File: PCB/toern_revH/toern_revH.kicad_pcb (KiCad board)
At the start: 4 copper layers, 160 x 71 mm, 130 parts, among them CN1 YZP0354-20100-01, CN2 YZP0354-20100-01, IC1 BQ24075TRGTR, J1 AudioJack3_Switch, J10 Conn_01x02, J11 Conn_01x05, J11.5 Conn_01x05, J12 Conn_01x05, J13 Conn_01x05, J14 Conn_01x05, J15 Conn_01x05, J16 Conn_01x02, J17 AudioJack3_Ground, J18 Conn_01x05_Socket, J19 Conn_01x05_Socket, J2 Conn_01x05_Socket, J20 Conn_01x05_Socket, J21 Conn_01x05_Socket, J22 Conn_01x05_Socket, J23 Conn_01x05_Socket, J24 Conn_01x05_Socket, J25 Conn_01x02, J26 Conn_01x02, J27 Conn_01x02, J28 929870-01-12-RA, J29 929870-01-12-RA, J3 AudioJack3_Ground, J30 929870-01-12-RA, J31 929870-01-12-RA, J4 USB_C_Receptacle_USB2.0, J5 AudioJack3_Switch, J6 AudioJack3_Switch, J7 AudioJack3_Switch, J8 Micro_SD_Card, J9 Conn_01x03, U1 SPX3819M5-L-3-3, U13 PAM8403D, U14 74LVC1G17, U15 74AHCT1G125, U16 74AHCT1G125, U2 SPX3819M5-L-1-8, U3 SGTL5000XNBA3, U4 TLP2361V4_E, U5 74LVC2G14, U6 Teensy4.1, U7 SPX3819M5-L-3-3, U8 TPS22918DBVR

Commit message: updated BAT45s Pins on PCB+Shematics
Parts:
- D2: value D_Schottky_Dual_Series_ACK -> BAT54S
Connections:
- D2 pad 2: Net-(D2-common) -> +3.3V
- D2 pad 3: +3.3V -> Net-(D2-common)
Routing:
- net Net-(D2-common): track 13.0 -> 11.5 mm
- net +3.3V: track 378.6 -> 377.5 mm, vias 17 -> 15
- net 38_CS1_IN1: track 17.9 -> 17.3 mm, vias 1 -> 0
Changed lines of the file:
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@@
 			)
 		)
-		(property "Value" "D_Schottky_Dual_Series_ACK"
+		(property "Value" "BAT54S"
 			(at 0 2.4 0)
 			(layer "F.Fab")
@@
 			)
 		)
-		(property "Datasheet" "~"
+		(property "Datasheet" "https://assets.nexperia.com/documents/data-sheet/BAT54S.pdf"
 			(at 0 0 0)
 			(layer "F.Fab")
@@
 			)
 		)
-		(property "Description" "Dual Schottky diode, anode/center/cathode"
+		(property "Description" "Dual series Schottky BAT54S: pin1=A, pin2=K, pin3=common"
 			(at 0 0 0)
 			(layer "F.Fab")
@@
 			(layers "F.Cu" "F.Mask" "F.Paste")
 			(roundrect_rratio 0.25)
-			(net 139 "Net-(D2-common)")
-			(pinfunction "common")
+			(net 7 "+3.3V")
+			(pinfunction "K")
 			(pintype "passive")
 		)
@@
 			(layers "F.Cu" "F.Mask" "F.Paste")
 			(roundrect_rratio 0.25)
-			(net 7 "+3.3V")
-			(pinfunction "K")
+			(net 139 "Net-(D2-common)")
+			(pinfunction "common")
 			(pintype "passive")
 		)
@@
 	)
 	(segment
+		(start 160.225 29.7)
+		(end 163.925 29.7)
+		(width 0.2)
+		(layer "F.Cu")
+		(net 7)
+	)
+	(segment
 		(start 72.5 50)
 		(end 73.5 50)
@@
 	)
 	(segment
+		(start 163.925 29.7)
+		(end 164.275 29.35)
+		(width 0.2)
+		(layer "F.Cu")
+		(net 7)
+	)
+	(segment
 		(start 161 66.25)
 		(end 178.125 66.25)
@@
 	)
 	(segment
-		(start 161.8 30.9)
-		(end 161.8 31.25)
-		(width 0.2)
-		(layer "F.Cu")
-		(net 7)
-	)
-	(segment
 		(start 184.6 66.25)
 		(end 187.55 63.3)
@@
 	)
 	(segment
-		(start 162.4 30.3)
-		(end 161.8 30.9)
-		(width 0.2)
-		(layer "F.Cu")
-		(net 7)
-	)
-	(segment
 		(start 118.22 75.78)
 		(end 118.22 77.5)
@@
 	)
 	(segment
-		(start 160.225 29.025)
-		(end 160.5 28.75)
-		(width 0.2)
-		(layer "F.Cu")
-		(net 7)
-	)
-	(segment
 		(start 121.22 75.505)
 		(end 121.225 75.5)
@@
 	)
 	(segment
-		(start 160.225 29.7)
-		(end 160.225 29.025)
-		(width 0.2)
-		(layer "F.Cu")
-		(net 7)
-	)
-	(segment
 		(start 117.325 80.325)
 		(end 118 81)
@@
 	)
 	(via
-		(at 161.8 31.25)
-		(size 0.5)
-		(drill 0.3)
-		(layers "F.Cu" "B.Cu")
-		(net 7)
-	)
-	(via
 		(at 146.465 39.615)
 		(size 0.5)
@@
 	)
 	(via
-		(at 160.5 28.75)
-		(size 0.5)
-		(drill 0.3)
-		(layers "F.Cu" "B.Cu")
-		(net 7)
-	)
-	(via
 		(at 143.7 51.45)
 		(size 0.5)
@@
 	)
 	(segment
-		(start 161.8 30.05)
-		(end 160.5 28.75)
-		(width 0.2)
-		(layer "B.Cu")
-		(net 7)
-	)
-	(segment
 		(start 72.5 50)
 		(end 72 50.5)
@@
 	)
 	(segment
-		(start 161.8 31.25)
-		(end 161.8 30.05)
-		(width 0.2)
-		(layer "B.Cu")
-		(net 7)
-	)
-	(segment
 		(start 80.5 41.69)
 		(end 82 40.19)
@@
 	)
 	(segment
-		(start 167.211918 31.947)
-		(end 167.581 31.577918)
-		(width 0.2)
-		(layer "F.Cu")
-		(net 90)
-	)
-	(segment
-		(start 160.225 31.6)
-		(end 160.95 31.6)
-		(width 0.2)
-		(layer "F.Cu")
-		(net 90)
-	)
-	(segment
-		(start 167.581 29.122082)
-		(end 167.158918 28.7)
+		(start 161.299 31.949)
+		(end 163.699644 31.949)
 		(width 0.2)
 		(layer "F.Cu")
@@
 	)
 	(segment
-		(start 163.701644 31.947)
-		(end 167.211918 31.947)
+		(start 163.07 28.7)
+		(end 161.28 26.91)
 		(width 0.2)
 		(layer "F.Cu")
@@
 	)
 	(segment
-		(start 162.3 28.7)
-		(end 162.3 28.85)
+		(start 167.158918 28.7)
+		(end 163.07 28.7)
 		(width 0.2)
 		(layer "F.Cu")
@@
 	)
 	(segment
-		(start 160.95 31.6)
-		(end 161.299 31.949)
+		(start 163.701644 31.947)
+		(end 167.211918 31.947)
 		(width 0.2)
 		(layer "F.Cu")
@@
 	)
 	(segment
-		(start 167.158918 28.7)
-		(end 162.3 28.7)
+		(start 167.581 29.122082)
+		(end 167.158918 28.7)
 		(width 0.2)
 		(layer "F.Cu")
@@
 	)
 	(segment
-		(start 163.699644 31.949)
-		(end 163.701644 31.947)
+		(start 167.211918 31.947)
+		(end 167.581 31.577918)
 		(width 0.2)
 		(layer "F.Cu")
@@
 	)
 	(segment
-		(start 161.299 31.949)
-		(end 163.699644 31.949)
+		(start 160.225 31.6)
+		(end 160.95 31.6)
 		(width 0.2)
 		(layer "F.Cu")
 		(net 90)
 	)
-	(via
-		(at 162.3 28.7)
-		(size 0.5)
-		(drill 0.3)
-		(layers "F.Cu" "B.Cu")
-		(net 90)
-	)
-	(segment
-		(start 162.25 27.88)
-		(end 161.28 26.91)
-		(width 0.2)
-		(layer "B.Cu")
-		(net 90)
-	)
 	(segment
-		(start 162.25 28.65)
-		(end 162.25 27.88)
+		(start 160.95 31.6)
+		(end 161.299 31.949)
 		(width 0.2)
-		(layer "B.Cu")
+		(layer "F.Cu")
 		(net 90)
 	)
 	(segment
-		(start 162.3 28.7)
-		(end 162.25 28.65)
+		(start 163.699644 31.949)
+		(end 163.701644 31.947)
 		(width 0.2)
-		(layer "B.Cu")
+		(layer "F.Cu")
 		(net 90)
 	)
@@
 	)
 	(segment
-		(start 166.56 30.7)
-		(end 164.7 30.7)
+		(start 167.11 31.25)
+		(end 166.56 30.7)
 		(width 0.2)
 		(layer "F.Cu")
@@
 	(segment
 		(start 164.7 30.7)
-		(end 164.275 30.275)
-		(width 0.2)
-		(layer "F.Cu")
-		(net 139)
-	)
-	(segment
-		(start 160.811954 30.65)
-		(end 162.111954 29.35)
+		(end 164.3 30.3)
 		(width 0.2)
 		(layer "F.Cu")
@@
 	)
 	(segment
-		(start 162.111954 29.35)
-		(end 164.275 29.35)
+		(start 166.56 30.7)
+		(end 164.7 30.7)
 		(width 0.2)
 		(layer "F.Cu")
@@
 	)
 	(segment
-		(start 167.11 31.25)
-		(end 166.56 30.7)
+		(start 162.4 30.3)
+		(end 160.811954 30.65)
 		(width 0.2)
 		(layer "F.Cu")
@@
 	)
 	(segment
-		(start 164.275 30.275)
-		(end 164.275 29.35)
+		(start 164.3 30.3)
+		(end 162.4 30.3)
 		(width 0.2)
 		(layer "F.Cu")

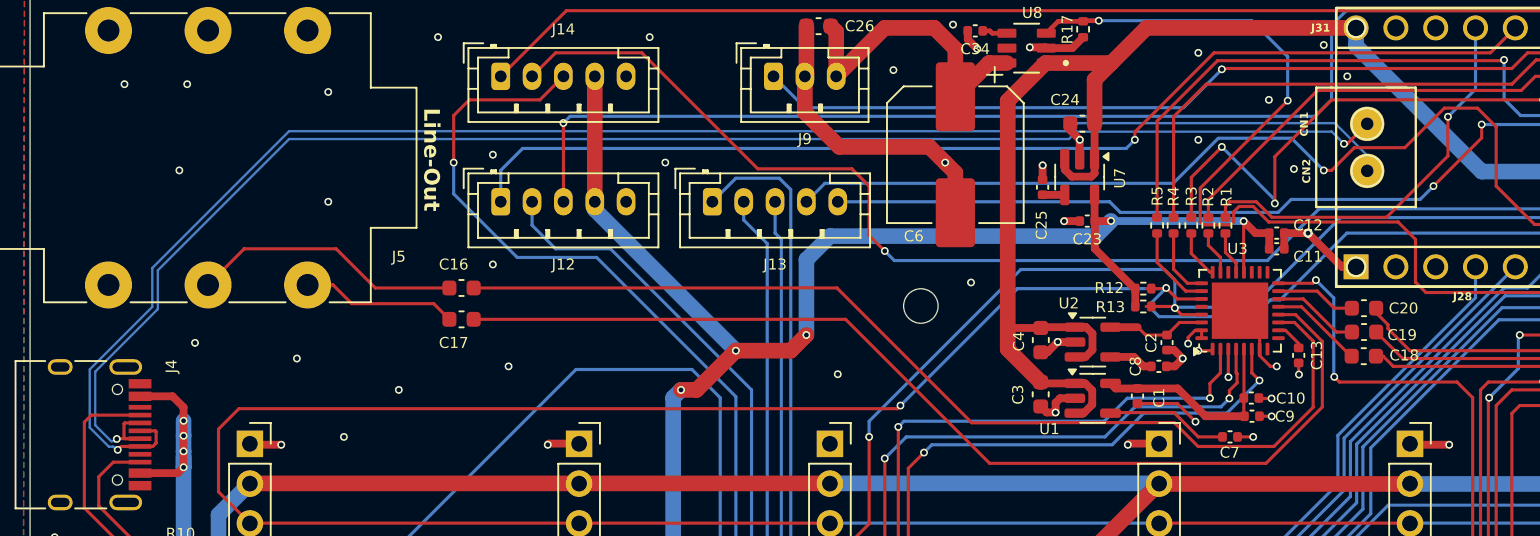
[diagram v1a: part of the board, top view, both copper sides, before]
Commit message: updated Pogopins position
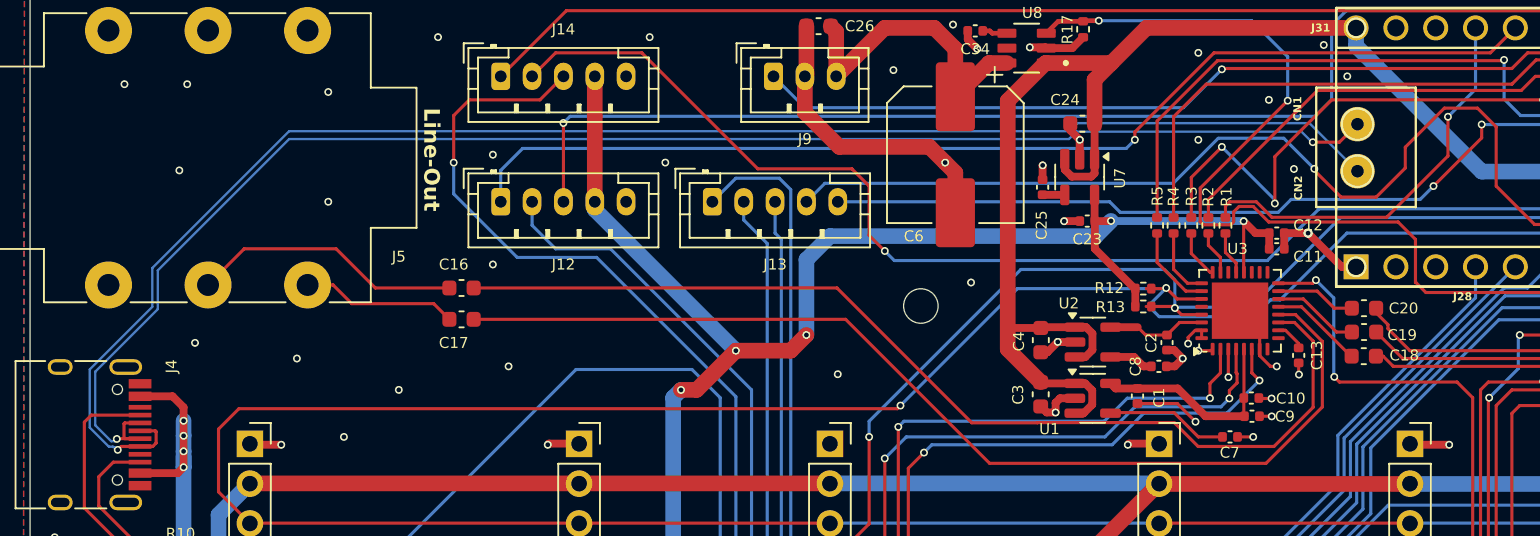
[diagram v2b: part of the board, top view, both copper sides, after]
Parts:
- moved CN1 0.62 mm to (115.7, 33.0)
- moved CN2 0.62 mm to (115.7, 36.0)
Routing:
- net 6_OUT1D: track 63.4 -> 65.7 mm
- net D+: track 101.8 -> 101.2 mm
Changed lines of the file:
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@@
 	(footprint "YZP0354-20100-01:YZP0354-20100-01"
 		(layer "F.Cu")
-		(at 116.27 33.03)
+		(at 115.65 33.05)
 		(descr "Xinyangze YZP0354-20100-01 through-hole pogo pin; EasyEDA UUID 717ea0c0017f4715b4b308a4536ca606")
 		(tags "pogo pin spring contact through-hole C5157282")
 		(property "Reference" "CN1"
-			(at -4.02 0.02 90)
+			(at -3.82 -0.98 90)
 			(layer "F.SilkS")
 			(effects
@@
 	(footprint "YZP0354-20100-01:YZP0354-20100-01"
 		(layer "F.Cu")
-		(at 116.27 36.03)
+		(at 115.65 36.05)
 		(descr "Xinyangze YZP0354-20100-01 through-hole pogo pin; EasyEDA UUID 717ea0c0017f4715b4b308a4536ca606")
 		(tags "pogo pin spring contact through-hole C5157282")
 		(property "Reference" "CN2"
-			(at -3.87 0.02 90)
+			(at -3.77 1.07 90)
 			(layer "F.SilkS")
 			(effects
@@
 		(sheetname "/")
 		(sheetfile "toern_revH.kicad_sch")
-		(attr through_hole exclude_from_pos_files exclude_from_bom)
+		(attr through_hole exclude_from_pos_files exclude_from_bom allow_missing_courtyard
+			dnp
+		)
 		(fp_line
 			(start -31.75 -3.81)
@@
 	)
 	(segment
-		(start 38.775 44.70401)
-		(end 38.775 42.225)
+		(start 38.775 42.225)
+		(end 47.5 33.5)
 		(width 0.15)
 		(layer "B.Cu")
@@
 	)
 	(segment
-		(start 36.00559 53.623078)
-		(end 34.785 52.402487)
+		(start 34.785 48.69401)
+		(end 38.775 44.70401)
 		(width 0.15)
 		(layer "B.Cu")
@@
 	)
 	(segment
-		(start 36.292537 53.655)
-		(end 36.260615 53.623078)
+		(start 115.36 36.05)
+		(end 115.65 36.05)
 		(width 0.15)
 		(layer "B.Cu")
@@
 	)
 	(segment
-		(start 36.398844 53.655)
-		(end 36.292537 53.655)
+		(start 47.5 33.5)
+		(end 97.252563 33.5)
 		(width 0.15)
 		(layer "B.Cu")
@@
 	)
 	(segment
-		(start 97.252563 33.5)
-		(end 97.767563 32.985)
+		(start 97.767563 32.985)
+		(end 112.585 32.985)
 		(width 0.15)
 		(layer "B.Cu")
@@
 	)
 	(segment
-		(start 36.571169 53.827325)
-		(end 36.398844 53.655)
+		(start 36.260615 53.623078)
+		(end 36.00559 53.623078)
 		(width 0.15)
 		(layer "B.Cu")
@@
 	)
 	(segment
-		(start 97.767563 32.985)
-		(end 114.212463 32.985)
+		(start 36.398844 53.655)
+		(end 36.292537 53.655)
 		(width 0.15)
 		(layer "B.Cu")
@@
 	)
 	(segment
-		(start 47.5 33.5)
-		(end 97.252563 33.5)
+		(start 112.585 32.985)
+		(end 115.63 36.03)
 		(width 0.15)
 		(layer "B.Cu")
@@
 	)
 	(segment
-		(start 36.260615 53.623078)
-		(end 36.00559 53.623078)
+		(start 97.252563 33.5)
+		(end 97.767563 32.985)
 		(width 0.15)
 		(layer "B.Cu")
@@
 	)
 	(segment
-		(start 34.785 48.69401)
-		(end 38.775 44.70401)
+		(start 115.63 36.03)
+		(end 115.98 36.03)
 		(width 0.15)
 		(layer "B.Cu")
@@
 	)
 	(segment
-		(start 38.775 42.225)
-		(end 47.5 33.5)
+		(start 38.775 44.70401)
+		(end 38.775 42.225)
 		(width 0.15)
 		(layer "B.Cu")
@@
 	)
 	(segment
-		(start 114.212463 32.985)
-		(end 116.27 35.042537)
+		(start 36.00559 53.623078)
+		(end 34.785 52.402487)
+		(width 0.15)
+		(layer "B.Cu")
+		(net 32)
+	)
+	(segment
+		(start 36.292537 53.655)
+		(end 36.260615 53.623078)
 		(width 0.15)
 		(layer "B.Cu")
@@
 	)
 	(segment
-		(start 116.27 35.042537)
-		(end 116.27 36.03)
+		(start 36.571169 53.827325)
+		(end 36.398844 53.655)
 		(width 0.15)
 		(layer "B.Cu")
@@
 	)
 	(segment
+		(start 112.8 34.2)
+		(end 114.5 34.2)
+		(width 0.2)
+		(layer "F.Cu")
+		(net 33)
+	)
+	(segment
+		(start 114.5 34.2)
+		(end 115.65 33.05)
+		(width 0.2)
+		(layer "F.Cu")
+		(net 33)
+	)
+	(segment
 		(start 36.97 52.16)
 		(end 36.97 53.06)
@@
 	)
 	(segment
-		(start 114.79 34.305)
-		(end 114.995 34.305)
+		(start 115.67 33.03)
+		(end 116.27 33.03)
 		(width 0.2)
 		(layer "F.Cu")
@@
 	)
 	(segment
-		(start 37.995 53.11)
-		(end 36.53 53.11)
+		(start 115.65 33.05)
+		(end 115.67 33.03)
 		(width 0.2)
 		(layer "F.Cu")
@@
 	)
 	(segment
-		(start 114.995 34.305)
-		(end 116.27 33.03)
+		(start 37.995 53.11)
+		(end 36.53 53.11)
 		(width 0.2)
 		(layer "F.Cu")
@@
 	)
 	(via
-		(at 114.79 34.305)
+		(at 112.8 34.2)
 		(size 0.5)
 		(drill 0.3)
@@
 	)
 	(segment
-		(start 39.125 42.375)
-		(end 47.5 34)
+		(start 35.135 48.838984)
+		(end 35.135 52.257512)
 		(width 0.15)
 		(layer "B.Cu")
@@
 	)
 	(segment
-		(start 97.247537 34)
+		(start 112.075 33.525)
 		(end 97.722537 33.525)
 		(width 0.15)
@@
 	)
 	(segment
-		(start 36.51 53.13)
-		(end 36.366922 53.273078)
+		(start 36.366922 53.273078)
+		(end 36.51 53.13)
 		(width 0.15)
 		(layer "B.Cu")
@@
 	)
 	(segment
-		(start 36.150566 53.273078)
-		(end 35.135 52.257512)
+		(start 112.8 34.2)
+		(end 112.75 34.2)
 		(width 0.15)
 		(layer "B.Cu")
@@
 	)
 	(segment
-		(start 97.722537 33.525)
-		(end 114.01 33.525)
+		(start 39.125 42.375)
+		(end 39.125 44.848984)
 		(width 0.15)
 		(layer "B.Cu")
@@
 	)
 	(segment
-		(start 114.01 33.525)
-		(end 114.79 34.305)
+		(start 35.135 52.257512)
+		(end 36.150566 53.273078)
 		(width 0.15)
 		(layer "B.Cu")
@@
 	)
 	(segment
-		(start 35.135 48.838984)
-		(end 39.125 44.848984)
+		(start 36.150566 53.273078)
+		(end 36.366922 53.273078)
 		(width 0.15)
 		(layer "B.Cu")
@@
 	)
 	(segment
-		(start 36.366922 53.273078)
-		(end 36.150566 53.273078)
+		(start 97.722537 33.525)
+		(end 97.247537 34)
 		(width 0.15)
 		(layer "B.Cu")
@@
 	(segment
 		(start 39.125 44.848984)
-		(end 39.125 42.375)
+		(end 35.135 48.838984)
 		(width 0.15)
 		(layer "B.Cu")
@@
 	(segment
 		(start 47.5 34)
-		(end 97.247537 34)
+		(end 39.125 42.375)
 		(width 0.15)
 		(layer "B.Cu")
@@
 	)
 	(segment
-		(start 35.135 52.257512)
-		(end 35.135 48.838984)
+		(start 97.247537 34)
+		(end 47.5 34)
+		(width 0.15)
+		(layer "B.Cu")
+		(net 33)
+	)
+	(segment
+		(start 112.75 34.2)
+		(end 112.075 33.525)
 		(width 0.15)
 		(layer "B.Cu")
@@
 	)
 	(segment
-		(start 121.19352 32.027248)
-		(end 123.30648 32.027248)
+		(start 114.6 37.7)
+		(end 116.85 37.7)
 		(width 0.2)
 		(layer "F.Cu")
@@
 	)
 	(segment
-		(start 118.670768 34.55)
-		(end 121.19352 32.027248)
+		(start 118.7 35.85)
+		(end 118.7 34.520768)
 		(width 0.2)
 		(layer "F.Cu")
@@
 	)
 	(segment
-		(start 132.65 42.15)
-		(end 133.34 42.15)
+		(start 129.949 39.449)
+		(end 132.65 42.15)
+		(width 0.2)
+		(layer "F.Cu")
+		(net 89)
+	)
+	(segment
+		(start 113 36)
+		(end 113 36.1)
 		(width 0.2)
 		(layer "F.Cu")
@@
 	)
 	(segment
-		(start 124.5 33.220768)
-		(end 124.5 37)
+		(start 116.85 37.7)
+		(end 118.7 35.85)
+		(width 0.2)
+		(layer "F.Cu")
+		(net 89)
+	)
+	(segment
+		(start 123.30648 32.027248)
+		(end 124.5 33.220768)
 		(width 0.2)
 		(layer "F.Cu")
@@
 	)
 	(segment
-		(start 115.45 34.55)
-		(end 118.670768 34.55)
+		(start 132.65 42.15)
+		(end 133.34 42.15)
 		(width 0.2)
 		(layer "F.Cu")
@@
 	)
 	(segment
-		(start 114 36)
-		(end 115.45 34.55)
+		(start 112.9 35.9)
+		(end 113 36)
+		(width 0.2)
+		(layer "F.Cu")
+		(net 89)
+	)
+	(segment
+		(start 118.7 34.520768)
+		(end 121.19352 32.027248)
 		(width 0.2)
 		(layer "F.Cu")
@@
 	)
 	(segment
-		(start 113.5 36)
-		(end 114 36)
+		(start 113 36.1)
+		(end 114.6 37.7)
 		(width 0.2)
 		(layer "F.Cu")
@@
 	)
 	(segment
-		(start 123.30648 32.027248)
-		(end 124.5 33.220768)
+		(start 124.5 33.220768)
+		(end 124.5 37)
 		(width 0.2)
 		(layer "F.Cu")
@@
 	)
 	(segment
-		(start 129.949 39.449)
-		(end 132.65 42.15)
+		(start 121.19352 32.027248)
+		(end 123.30648 32.027248)
 		(width 0.2)
 		(layer "F.Cu")
@@
 	)
 	(via
-		(at 113.5 36)
+		(at 112.9 35.9)
 		(size 0.5)
 		(drill 0.3)
@@
 	)
 	(segment
-		(start 103.896768 36.824)
+		(start 110.949 33.949)
 		(end 106.771768 33.949)
 		(width 0.2)
@@
 	)
 	(segment
-		(start 106.771768 33.949)
-		(end 111.449 33.949)
+		(start 112.9 35.9)
+		(end 110.949 33.949)
 		(width 0.2)
 		(layer "B.Cu")
@@
 	)
 	(segment
-		(start 81.676 36.824)
+		(start 106.771768 33.949)
 		(end 103.896768 36.824)
 		(width 0.2)
@@
 	)
 	(segment
-		(start 111.449 33.949)
-		(end 113.5 36)
+		(start 81.676 36.824)
+		(end 80.5 38)
 		(width 0.2)
 		(layer "B.Cu")
@@
 	)
 	(segment
-		(start 80.5 38)
+		(start 103.896768 36.824)
 		(end 81.676 36.824)
 		(width 0.2)

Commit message: finalized exttouch-modular version
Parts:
- J12 - BUTTON_A-C: renamed from J12
- J13 - TOUCHYTOUCH: renamed from J13
- J14 + BUTTON_C: renamed from J14
- renumbered J11 to J11-3.3V, J11.5 to J11-5V
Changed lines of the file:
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@@
 		(descr "JST PH series connector, B5B-PH-K (http://www.jst-mfg.com/product/pdf/eng/ePH.pdf), generated with kicad-footprint-generator")
 		(tags "connector JST PH side entry")
-		(property "Reference" "J11.5"
+		(property "Reference" "J11-5V"
 			(at 3.5 -3.1 0)
 			(layer "F.SilkS")
@@
 		(tags "capacitor")
 		(property "Reference" "C16"
-			(at 0.5 1.5 180)
+			(at -2.8 -0.65 180)
 			(layer "F.SilkS")
 			(effects
@@
 		(descr "JST PH series connector, B5B-PH-K (http://www.jst-mfg.com/product/pdf/eng/ePH.pdf), generated with kicad-footprint-generator")
 		(tags "connector JST PH side entry")
-		(property "Reference" "J11"
+		(property "Reference" "J11-3.3V"
 			(at 4 -3 0)
 			(layer "F.SilkS")
@@
 		(descr "JST PH series connector, B5B-PH-K (http://www.jst-mfg.com/product/pdf/eng/ePH.pdf), generated with kicad-footprint-generator")
 		(tags "connector JST PH side entry")
-		(property "Reference" "J12"
+		(property "Reference" "J12 - BUTTON_A-C"
 			(at 4 4 0)
 			(layer "F.SilkS")
@@
 		(tags "capacitor")
 		(property "Reference" "C17"
-			(at 0.5 -1.5 180)
+			(at -2.7 -0.75 180)
 			(layer "F.SilkS")
 			(effects
@@
 		(descr "JST PH series connector, B5B-PH-K (http://www.jst-mfg.com/product/pdf/eng/ePH.pdf), generated with kicad-footprint-generator")
 		(tags "connector JST PH side entry")
-		(property "Reference" "J13"
+		(property "Reference" "J13 - TOUCHYTOUCH"
 			(at 4 4 0)
 			(layer "F.SilkS")
@@
 		(descr "JST PH series connector, B5B-PH-K (http://www.jst-mfg.com/product/pdf/eng/ePH.pdf), generated with kicad-footprint-generator")
 		(tags "connector JST PH side entry")
-		(property "Reference" "J14"
+		(property "Reference" "J14 + BUTTON_C"
 			(at 4 -3 0)
 			(layer "F.SilkS")
